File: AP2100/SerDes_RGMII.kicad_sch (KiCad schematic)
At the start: 66 parts, among them U10 LS1043ASE7KQB-Layerscape

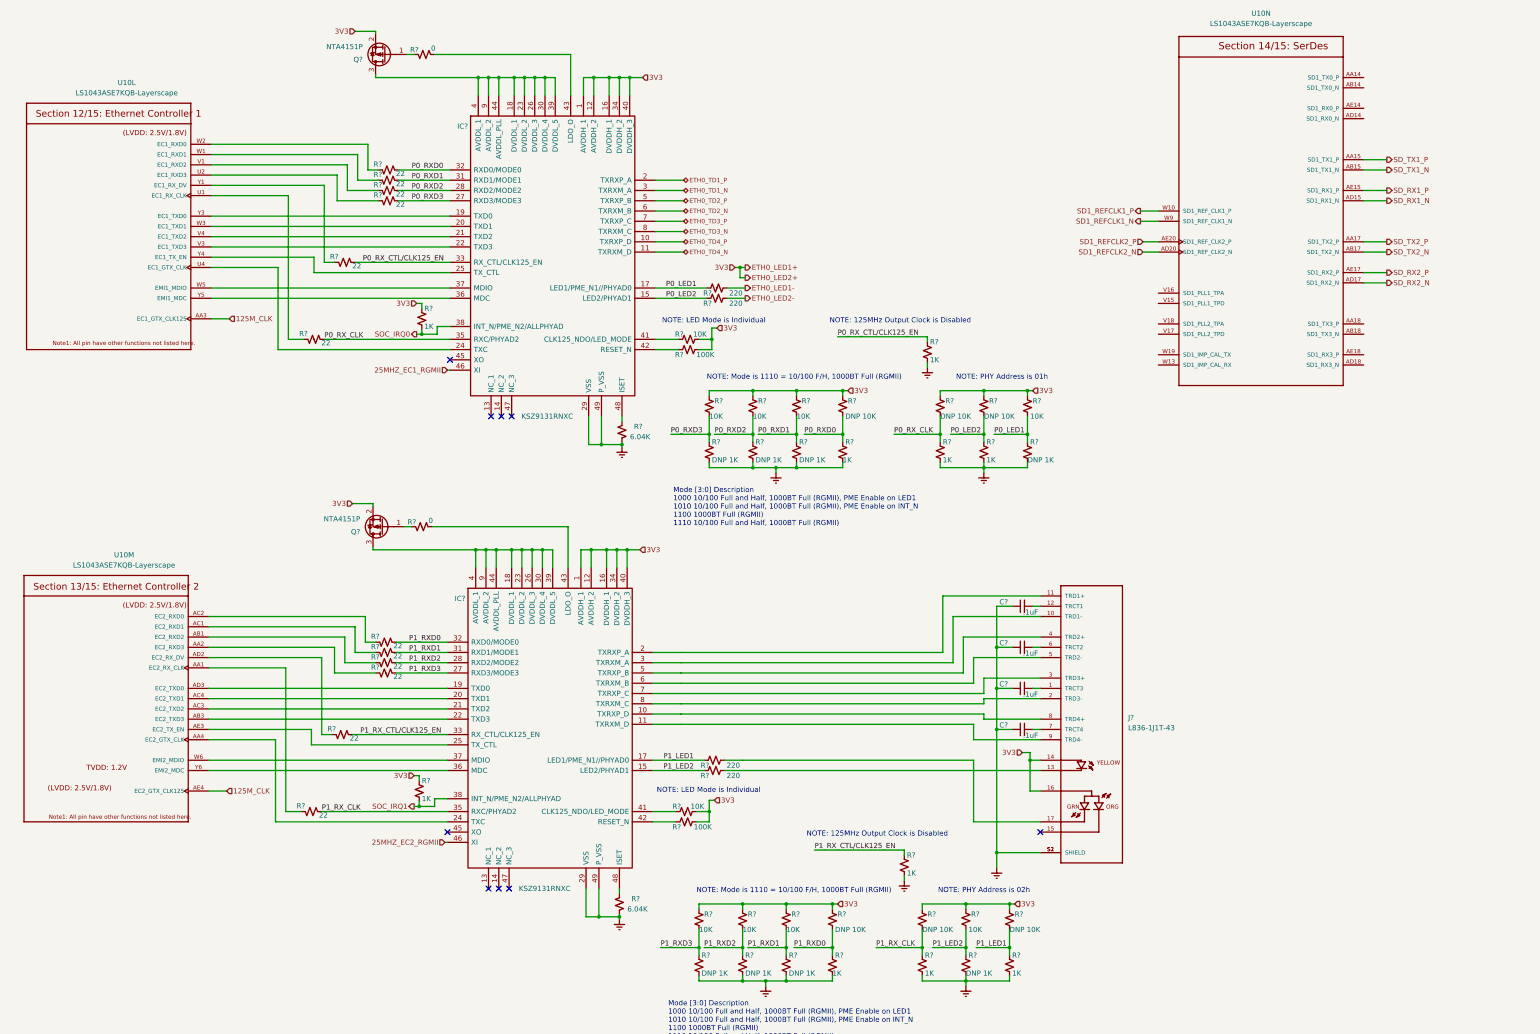
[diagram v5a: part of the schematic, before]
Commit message: Review / cleanup footprints, etc
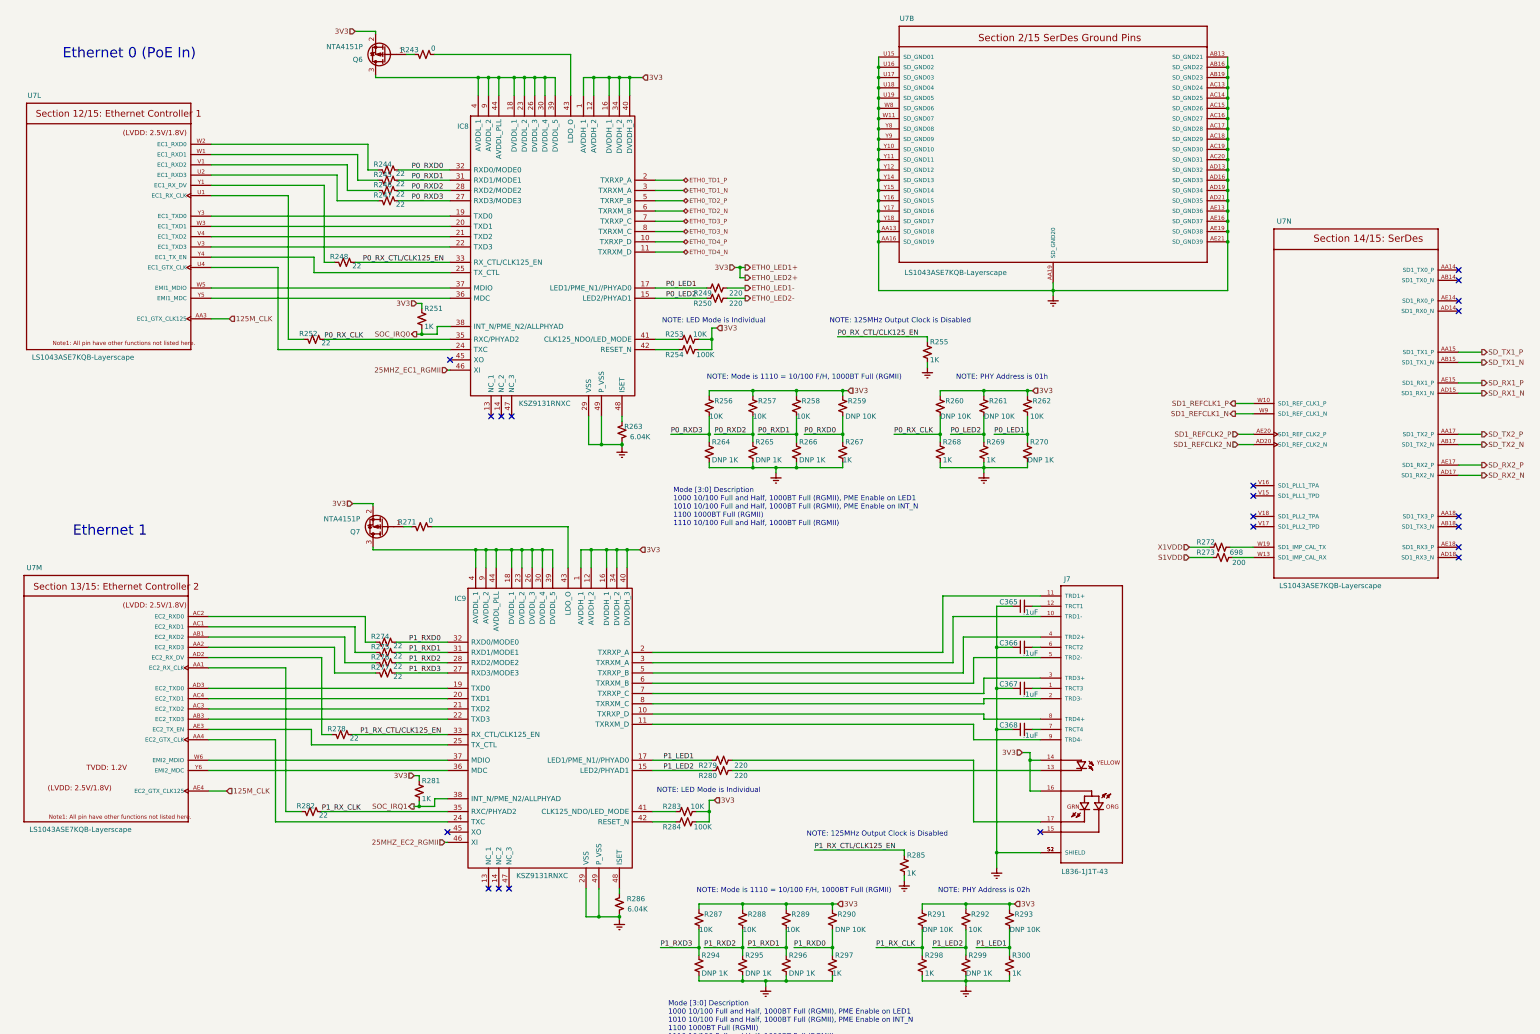
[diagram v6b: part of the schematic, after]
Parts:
- added R272: 698, Resistor_SMD:R_0402_1005Metric, symbol Device:R_Small_US
- added R273: 200, Resistor_SMD:R_0402_1005Metric, symbol Device:R_Small_US
- added unit 2 of U7
- gave numbers to parts that had none: 65
- renumbered U10 to U7
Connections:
- net GND: now also U7.AA13 (SD_GND18), U7.AA16 (SD_GND19), U7.AA19 (SD_GND20), U7.AB13 (SD_GND21), U7.AB16 (SD_GND22), U7.AB19 (SD_GND23), U7.AC13 (SD_GND24), U7.AC14 (SD_GND25), U7.AC15 (SD_GND26), U7.AC16 (SD_GND27), U7.AC17 (SD_GND28), U7.AC18 (SD_GND29), U7.AC19 (SD_GND30), U7.AC20 (SD_GND31), U7.AD13 (SD_GND32), U7.AD16 (SD_GND33), U7.AD19 (SD_GND34), U7.AD21 (SD_GND35), U7.AE13 (SD_GND36), U7.AE16 (SD_GND37), U7.AE19 (SD_GND38), U7.AE21 (SD_GND39), U7.U15 (SD_GND01), U7.U16 (SD_GND02), U7.U17 (SD_GND03), U7.U18 (SD_GND04), U7.U19 (SD_GND05), U7.W11 (SD_GND07), U7.W8 (SD_GND06), U7.Y10 (SD_GND10), U7.Y11 (SD_GND11), U7.Y12 (SD_GND12), U7.Y14 (SD_GND13), U7.Y15 (SD_GND14), U7.Y16 (SD_GND15), U7.Y17 (SD_GND16), U7.Y18 (SD_GND17), U7.Y8 (SD_GND08), U7.Y9 (SD_GND09)
- net at U7.W13 (SD1_IMP_CAL_RX): now also R273.2
- net at U7.W19 (SD1_IMP_CAL_TX): now also R272.2
- new net S1VDD: R273.1
- new net X1VDD: R272.1
- no-connect marks 9 -> 21
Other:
- note added: "Ethernet 0 (PoE In)"
- note added: "Ethernet 1"
- moved on the sheet: R279, R280, U7N

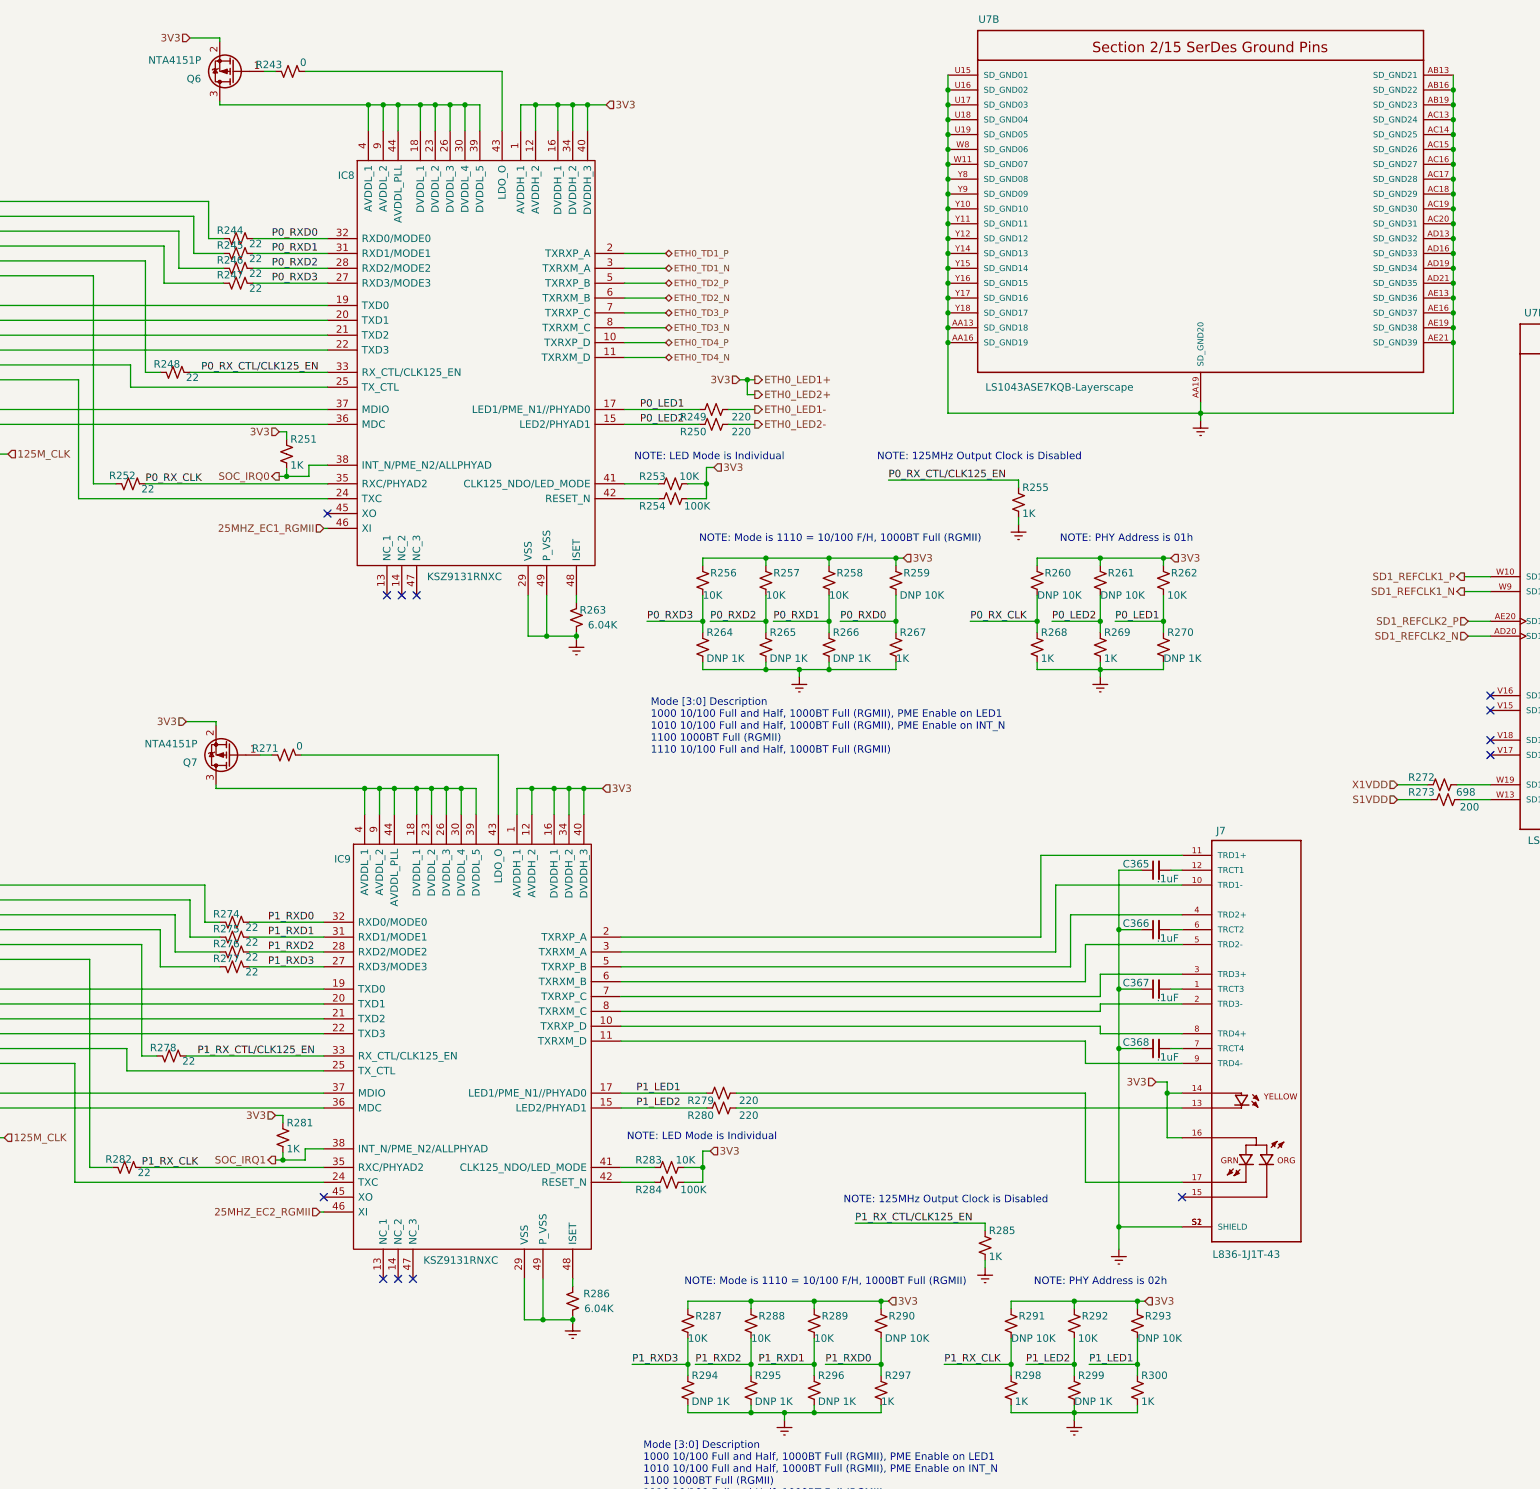
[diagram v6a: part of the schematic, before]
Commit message: Added antenna mounting holes
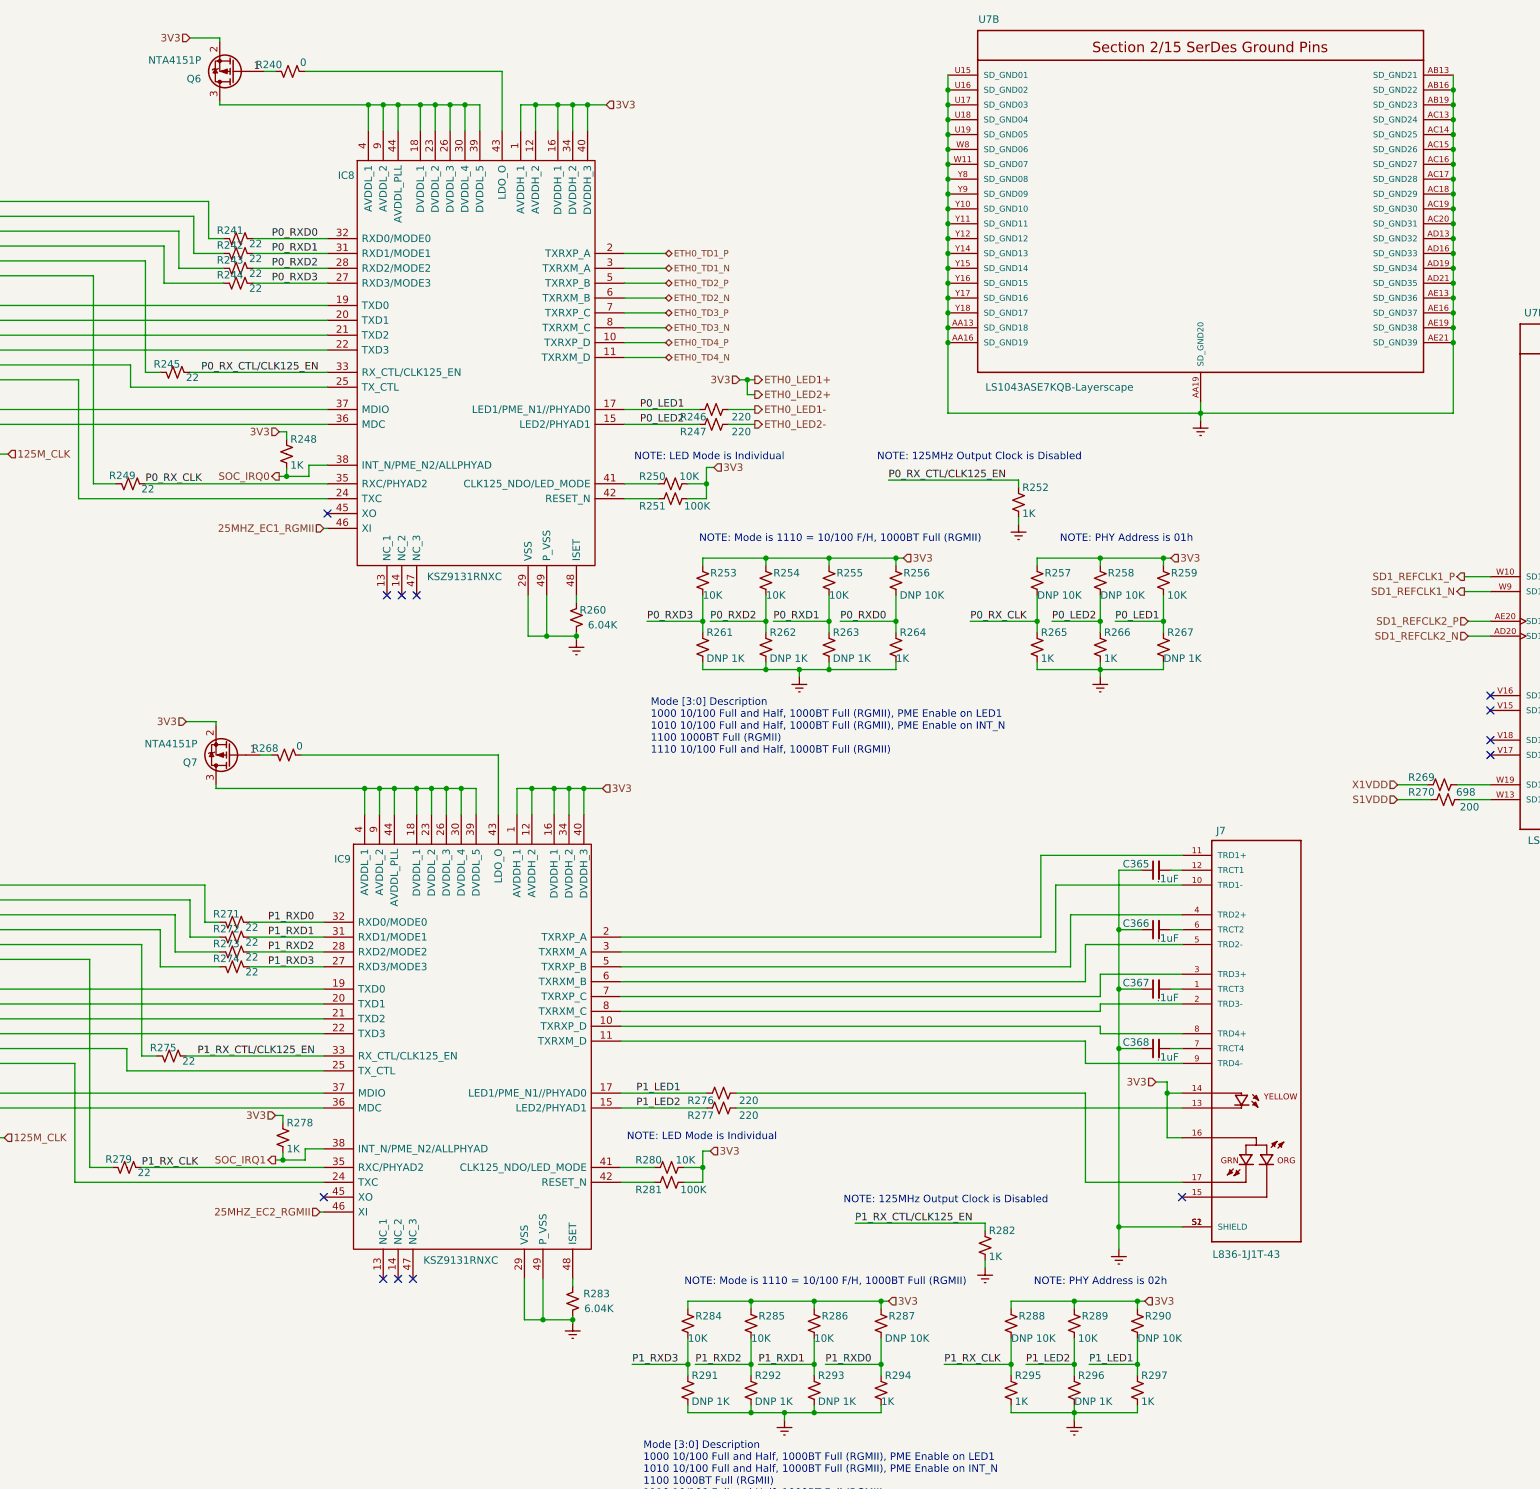
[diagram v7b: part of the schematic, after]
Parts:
- renumbered R243 to R240, R244 to R241, R245 to R242, R246 to R243, R247 to R244, R248 to R245, R249 to R246, R250 to R247, R251 to R248, R252 to R249, R253 to R250, R254 to R251, R255 to R252, R256 to R253, R257 to R254, R258 to R255, R259 to R256, R260 to R257, R261 to R258, R262 to R259, R263 to R260, R264 to R261, R265 to R262, R266 to R263, R267 to R264, R268 to R265, R269 to R266, R270 to R267, R271 to R268, R272 to R269, R273 to R270, R274 to R271, R275 to R272, R276 to R273, R277 to R274, R278 to R275, R279 to R276, R280 to R277, R281 to R278, R282 to R279, R283 to R280, R284 to R281, R285 to R282, R286 to R283, R287 to R284, R288 to R285, R289 to R286, R290 to R287, R291 to R288, R292 to R289, R293 to R290, R294 to R291, R295 to R292, R296 to R293, R297 to R294, R298 to R295, R299 to R296, R300 to R297
